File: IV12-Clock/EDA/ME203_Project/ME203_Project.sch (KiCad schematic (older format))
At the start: 23 parts, among them J1 Conn_01x12, J2 Conn_01x05, J6 Conn_01x07

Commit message: Code KWS, working on actual time.
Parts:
- added J10, J12: Conn_01x01, Connector_PinHeader_2.54mm:PinHeader_1x01_P2.54mm_Vertical, symbol Connector_Generic:Conn_01x01
- added J11, J13: Conn_01x02, Connector_PinHeader_2.54mm:PinHeader_1x02_P2.54mm_Vertical, symbol Connector_Generic:Conn_01x02
- J1: footprint Connector_PinSocket_2.54mm:PinSocket_1x12_P2.54mm_Vertical -> Connector_PinSocket_2.54mm:PinSocket_2x06_P2.54mm_Vertical
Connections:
- net +3V3: now also J11.1 (Pin_1), J11.2 (Pin_2)
- net GND: now also J13.1 (Pin_1), J13.2 (Pin_2)
- net ESP32/A0-DAC2 renamed DAC2
- net ESP32/A1-DAC1 renamed DAC1
- net ESP32/A9-D33 renamed ESP32/A9-T8-D33
- new net ESP32/A11-T5-D12: J12.1 (Pin_1)
- new net ESP32/A7-T9-D32: J10.1 (Pin_1)
- no-connect marks 2 -> 0
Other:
- note added: "Can interfere \nwith boot if pull \ndown affected"
- note removed: "Can interfere \nwith boot"
- note removed: "Unused but\navailable."
- moved on the sheet: J1, J6, R10, R11, R12, R13, R14, R15, R4, R5, R6, R7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

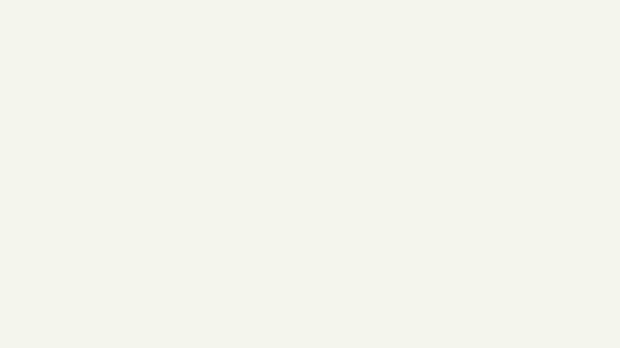
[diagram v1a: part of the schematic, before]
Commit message: Added touch buttons for speakers (untested)
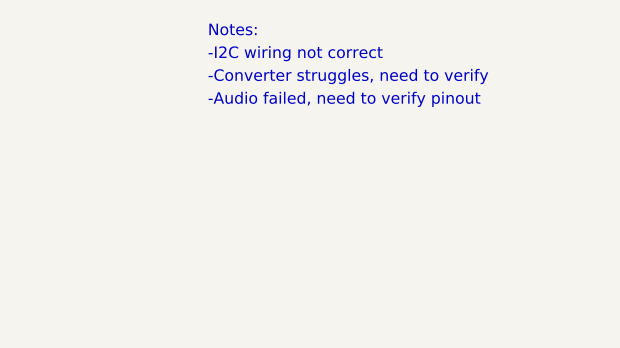
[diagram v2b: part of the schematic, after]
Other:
- note added: "-Audio failed, need to verify pinout"
- note added: "-Converter struggles, need to verify"
- note added: "-I2C wiring not correct"
- note added: "Notes:"
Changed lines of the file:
@@
 	1    0    0    -1
 $EndComp
+Text Notes 9750 700  0    50   ~ 0
+Notes:
+Text Notes 9750 800  0    50   ~ 0
+-I2C wiring not correct
+Text Notes 9750 900  0    50   ~ 0
+-Converter struggles, need to verify
+Text Notes 9750 1000 0    50   ~ 0
+-Audio failed, need to verify pinout
 $EndSCHEMATC
